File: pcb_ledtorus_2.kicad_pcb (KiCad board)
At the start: 4 copper layers, 149 x 149 mm, 277 parts, among them P1 CONN_02X04, P2 CONN_6, P3 MICRO-SD, P4 CONN_2, P5 KNUSB, P6 CONN_12, U1 STM32F46X_LQFP176, U10 TLC5955, U11 TLC5955, U12 TLC5955, U13 TLC5955, U14 TLC5955, U15 TLC5955, U3 LP38691, U4 TLC5955, U5 TLC5955, U6 TLC5955, U7 TLC5955, U8 TLC5955, U9 TLC5955, X1 MA-505

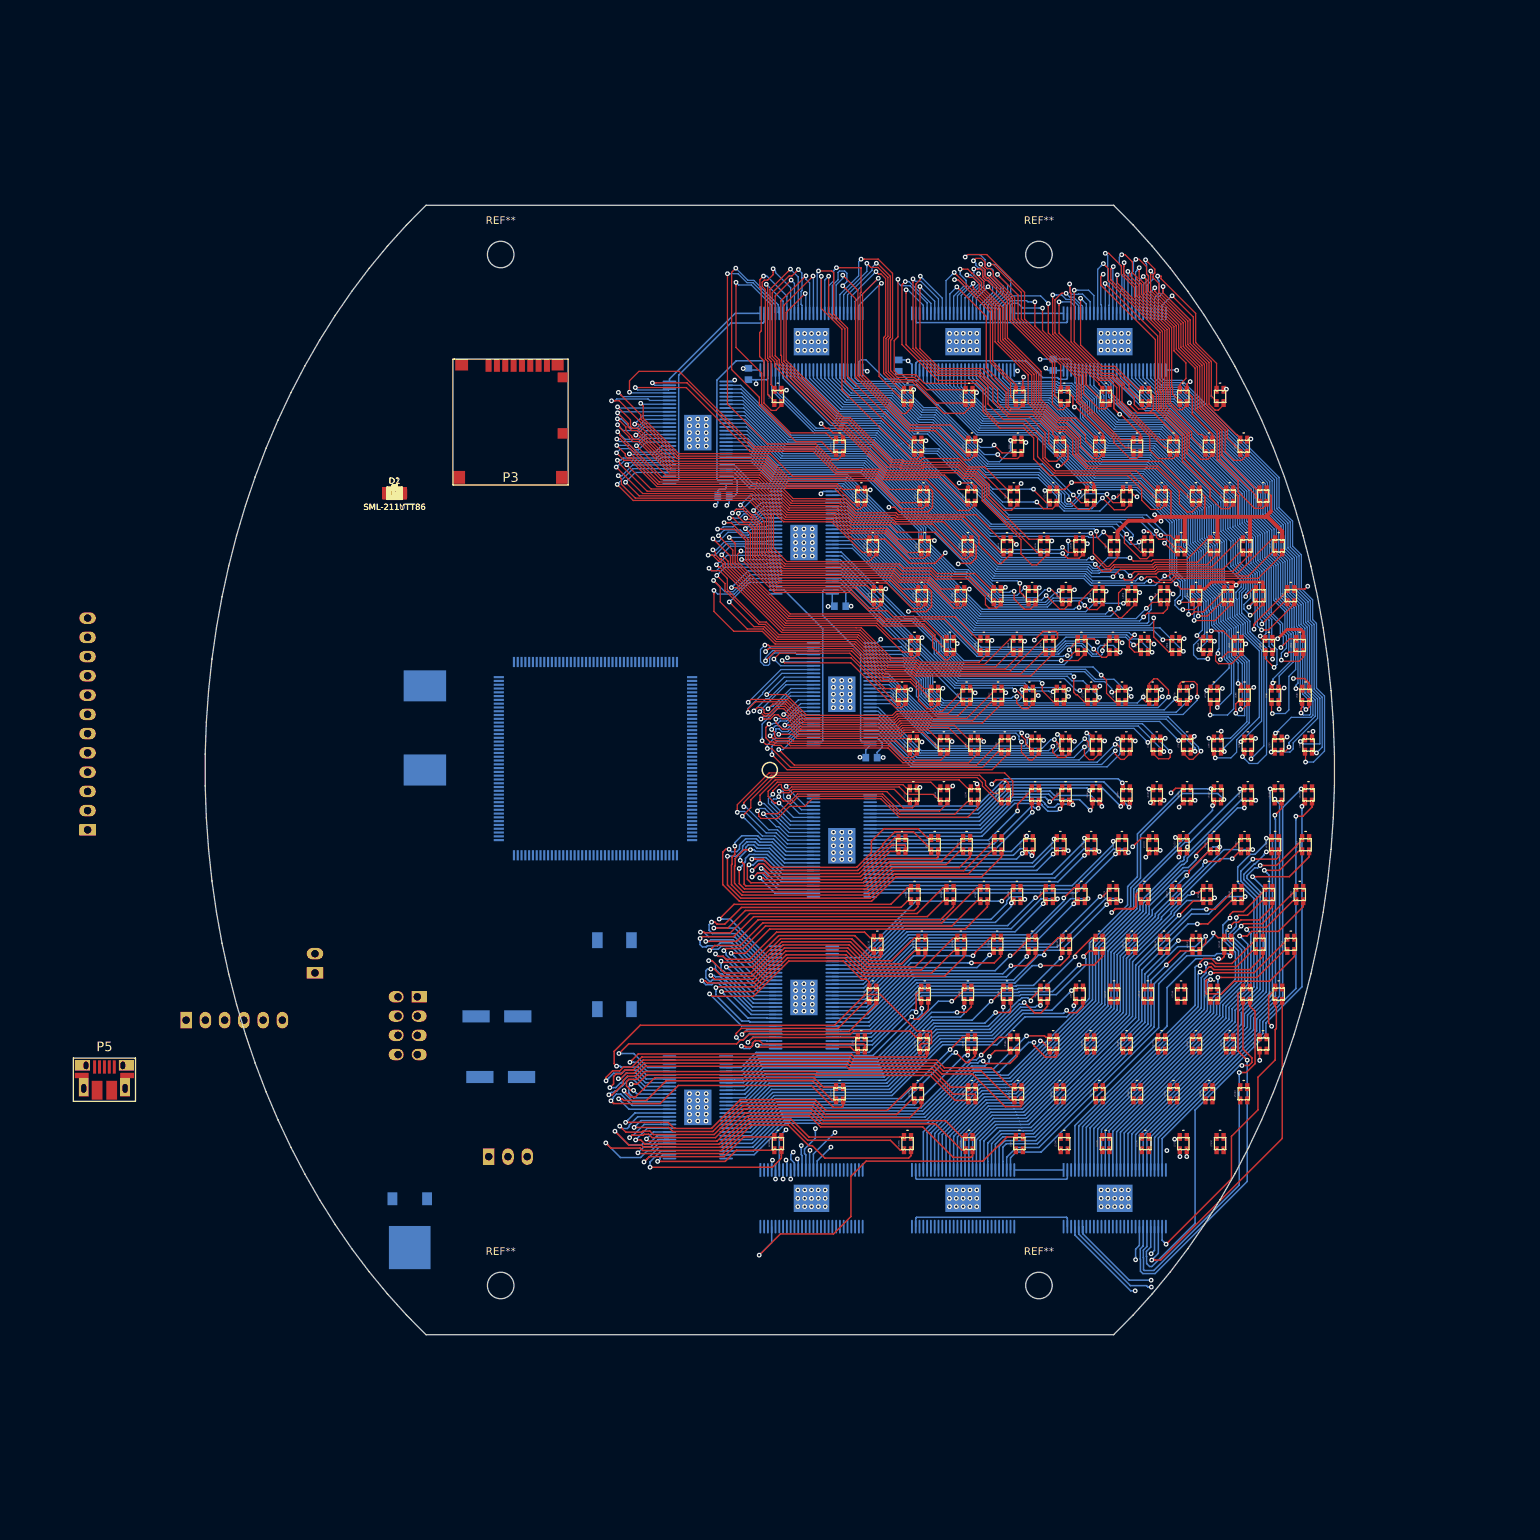
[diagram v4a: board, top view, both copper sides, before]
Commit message: Small component changes.
Fix couple of missing footprints. Make 100nF caps 0603.

Some very rough component placement to avoid overlap.
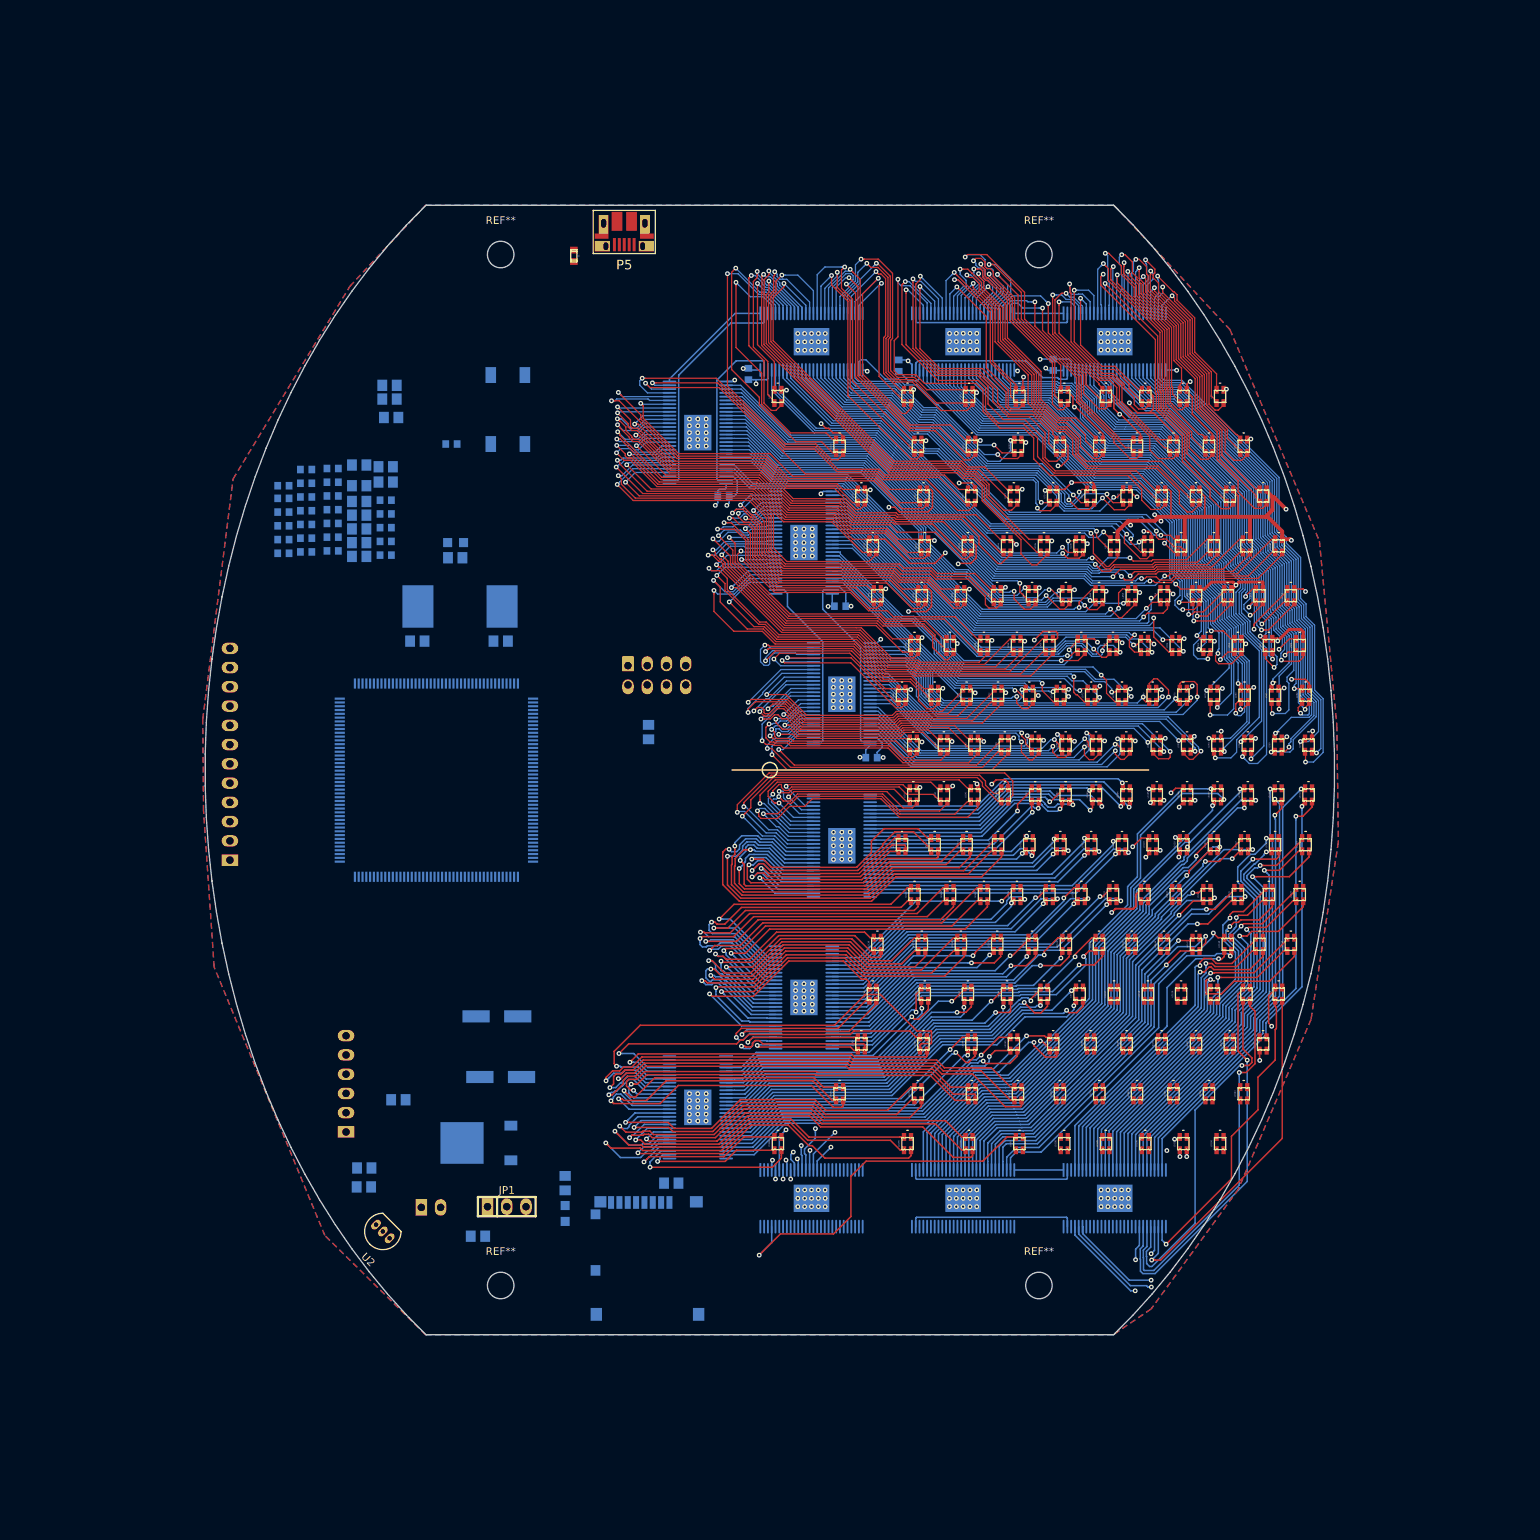
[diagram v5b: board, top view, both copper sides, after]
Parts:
- added L1: 30@100MHz, w_smd_cap:c_0603, F.Cu at (124.2, 82.2)
- added U2: US4881_HALL, TO_SOT_Packages_THT:TO-92_Inline_Narrow_Oval, F.Cu at (99.8, 211.8)
- C1, C10, C11, C12, C13, C14, C15, C16, C17, C18, C19, C2, C25, C29, C4, C5, C6, C7, C8, C9: footprint w_smd_cap:c_0805 -> w_smd_cap:c_0603; moved to B.Cu
- C20, C21, C22, C23, C24, C26, C27, C28, C3, C30, C31, C40, C41, C42, C43, C44, C45, D1, D2, P3, R1, R10, R11, R2, R3, R4, R5, R6, R7, R8, R9: moved to B.Cu
- JP1: moved to F.Cu
- moved P5 133.1 mm to (130.8, 77.9), turned to 180 degrees
- moved P3 111.9 mm to (133.9, 214.2), turned to 0 degrees
- moved R8 98.6 mm to (111.5, 211.5), turned to 180 degrees
- moved R1 98.0 mm to (137.0, 204.5), turned to 180 degrees
- moved D1 97.6 mm to (123.0, 208.5), turned to 90 degrees
- moved R6 93.7 mm to (123.0, 204.5), turned to 90 degrees
- moved C3 91.6 mm to (96.5, 205.0)
- moved R2 89.1 mm to (96.5, 202.5)
- moved R4 80.0 mm to (101.0, 193.5)
- moved B1 75.9 mm to (115.4, 102.5), turned to 180 degrees
- moved P1 56.7 mm to (135.1, 137.5), turned to 0 degrees
- moved R5 46.0 mm to (134.0, 145.0), turned to 90 degrees
- moved P4 35.7 mm to (105.3, 207.7), turned to 0 degrees
- moved C31 24.0 mm to (114.5, 133.0), turned to 180 degrees
- moved U1 21.2 mm to (106.0, 151.3), turned to 0 degrees
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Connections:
- net /vusb renamed /vusb_mcu
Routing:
- net +5V: track 222.8 -> 227.3 mm, vias 85 -> 88
- net /LEDs/led22b: track 58.4 -> 54.4 mm
- net /LEDs/led23b: track 49.4 -> 52.7 mm
- net /LEDs/led23r: track 58.7 -> 61.0 mm
- net /LEDs/led22r: track 56.8 -> 54.5 mm
- net /LEDs/led23g: track 55.7 -> 57.9 mm
- net /LEDs/led12b: track 41.7 -> 39.5 mm
- net /LEDs/led24r: track 39.8 -> 41.8 mm
- net /LEDs/led11b: track 34.4 -> 36.3 mm
- net /LEDs/led96b: track 63.2 -> 61.8 mm
- net /LEDs/led1b: track 19.1 -> 20.6 mm
- net /LEDs/led1r: track 27.1 -> 28.5 mm
- net /LEDs/led10r: track 45.1 -> 43.7 mm
- net /LEDs/led24g: track 37.6 -> 38.9 mm
- net /LEDs/led11g: track 33.1 -> 34.2 mm
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- added copper zone on B.Cu, net GND
- added copper zone on F.Cu, net GND

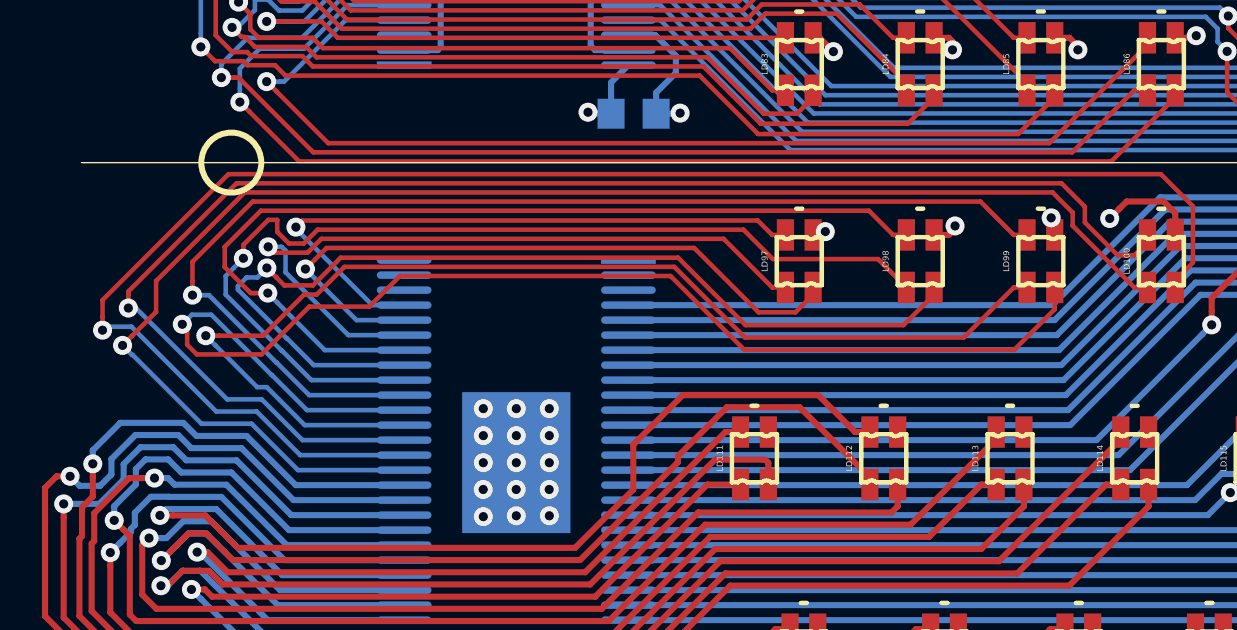
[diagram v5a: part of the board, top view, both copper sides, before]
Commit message: Fix so that DRC passes (with lots of unconnected)
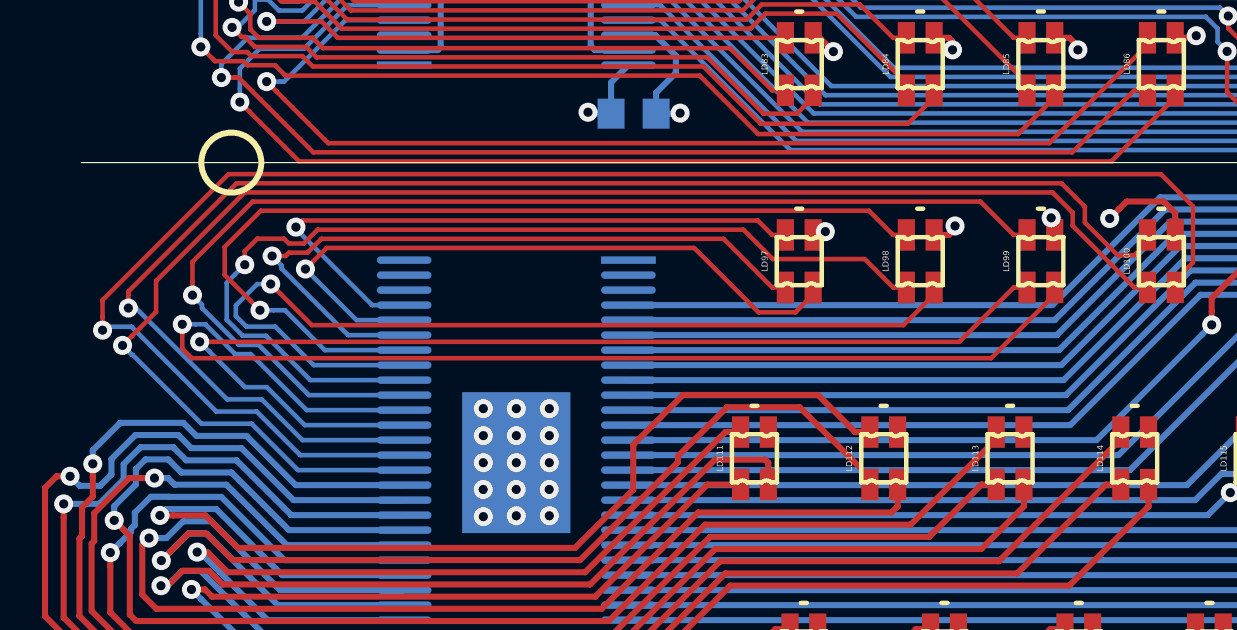
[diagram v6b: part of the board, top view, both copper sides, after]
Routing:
- net /LEDs/led99r: track 42.2 -> 39.7 mm
- net /LEDs/led99g: track 37.8 -> 36.3 mm
- net /LEDs/led98r: track 32.4 -> 31.4 mm
- net /LEDs/led97g: track 24.4 -> 23.6 mm
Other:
- net class LEDs added: clearance 0.1524, trace_width 0.1524, via_dia 0.635, via_drill 0.3048

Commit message: First rough component placement, looks ok.
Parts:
- moved C45 129.8 mm to (186.2, 210.8)
- moved C44 116.1 mm to (168.8, 214.8)
- moved C43 114.4 mm to (147.0, 212.5)
- moved C2 100.0 mm to (134.0, 204.8), turned to 270 degrees
- moved C1 99.1 mm to (102.5, 208.5), turned to 315 degrees
- moved C42 81.2 mm to (130.2, 184.0)
- moved C41 80.9 mm to (138.0, 177.0)
- moved R3 79.5 mm to (120.0, 186.8), turned to 270 degrees
- moved C4 77.6 mm to (124.8, 186.7), turned to 270 degrees
- moved C23 69.7 mm to (110.2, 188.2)
- moved C28 69.5 mm to (97.5, 168.8), turned to 90 degrees
- moved C40 68.2 mm to (143.0, 157.2)
- moved C24 66.3 mm to (109.8, 177.5)
- moved C12 57.3 mm to (124.0, 159.8)
- moved C16 55.6 mm to (94.0, 167.5)
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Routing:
- net +5V: track 227.3 -> 260.4 mm, vias 88 -> 91
- net /Power/bat_vcc: track 0.00 -> 4.48 mm
- net +3V3: track 29.6 -> 33.6 mm
- added copper zone on In1.Cu, net +3V3
